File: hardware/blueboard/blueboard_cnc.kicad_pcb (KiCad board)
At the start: 2 copper layers, 199.4 x 198.9 mm, 105 parts, among them SW1 SW_SPST

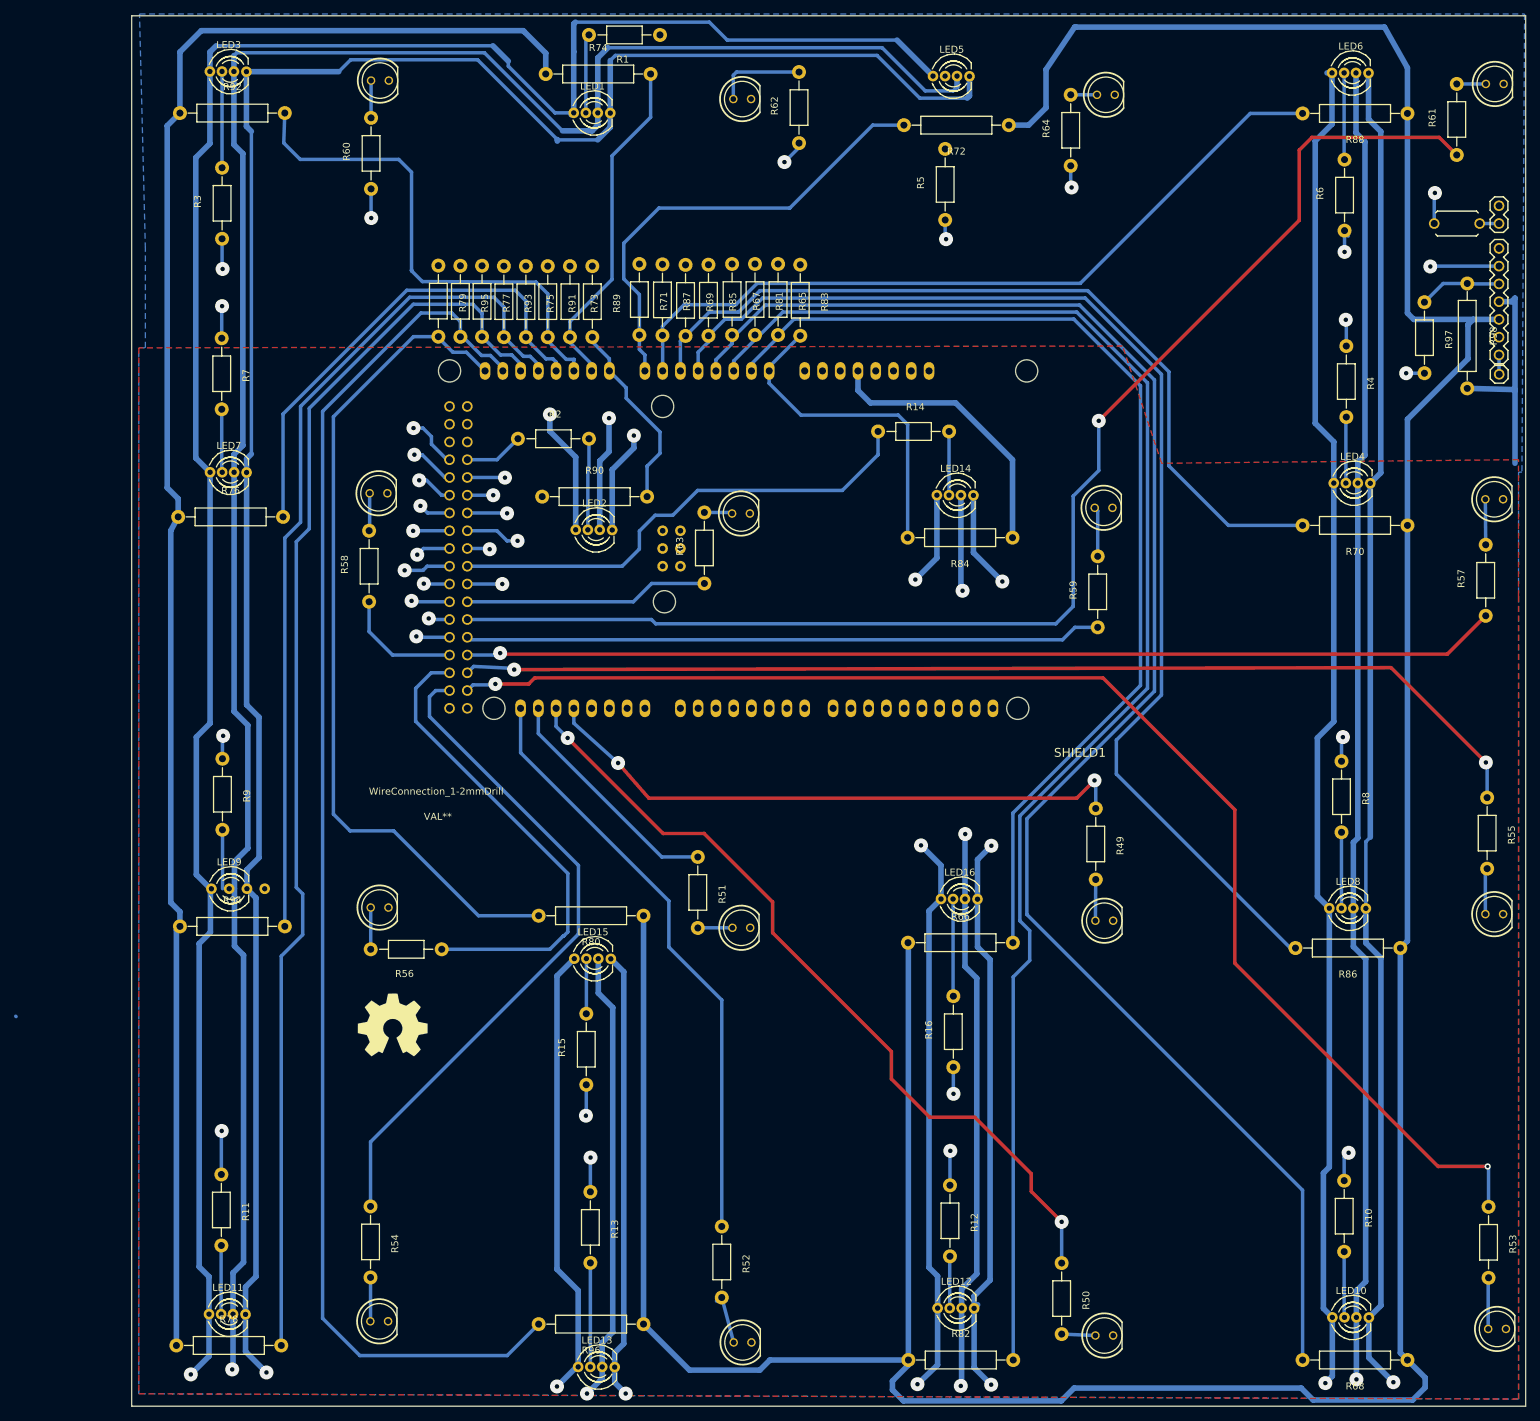
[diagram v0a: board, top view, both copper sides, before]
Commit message: state when board was cncd
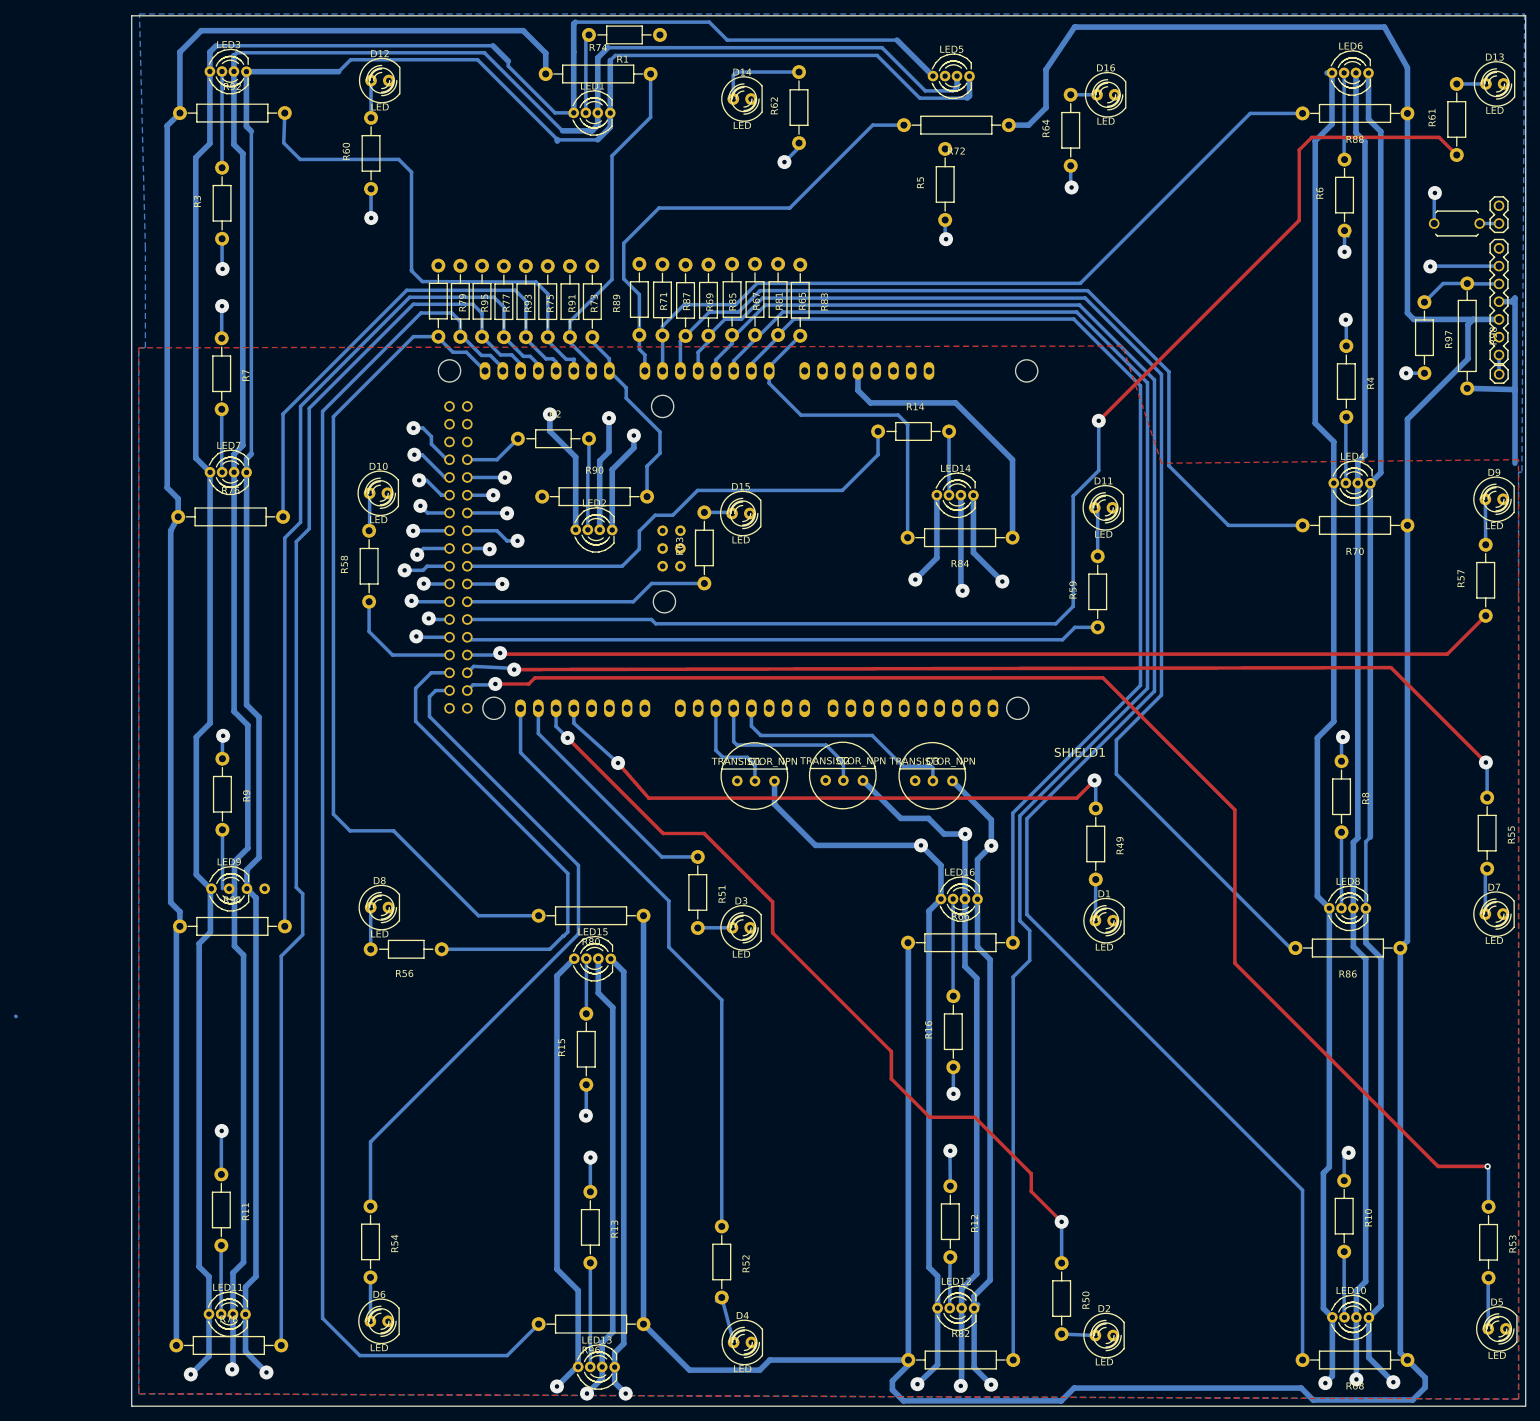
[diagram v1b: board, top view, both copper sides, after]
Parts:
- removed LOGO_OSHW_silkscreen_10mm: val**, Freetronics:LOGO_OSHW_silkscreen_10mm
- removed WireConnection_1-2mmDrill: VAL**, Wire_Connections_Bridges:WireConnection_1-2mmDrill
- added Q1: TRANSISTOR_NPN, finn_kicad:EBC-transistor-NPN, F.Cu at (186.7, 22.1)
- added Q2: TRANSISTOR_NPN, finn_kicad:EBC-transistor-NPN, F.Cu at (199.3, 22.0)
- added Q3: TRANSISTOR_NPN, finn_kicad:EBC-transistor-NPN, F.Cu at (212.1, 22.1)
- D1, D10, D11, D12, D13, D14, D15, D16, D2, D3, D4, D5, D6, D7, D8, D9: footprint Freetronics:LED-5MM -> LEDs:LED-5MM
- R1, R10, R11, R12, R13, R14, R15, R16, R2, R3, R4, R5, R6, R7, R8, R9: value 470 -> 220
- moved R12 0.14 mm to (214.6, 87.9)
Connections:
- R1 pad 2: Net-(LED1-PadA) -> Net-(LED16-PadA)
- R10 pad 2: Net-(LED10-PadA) -> Net-(LED9-PadA)
- R11 pad 2: Net-(LED11-PadA) -> Net-(LED10-PadA)
- R12 pad 2: Net-(LED12-PadA) -> Net-(LED11-PadA)
- R13 pad 1: Net-(R13-Pad1) -> Net-(LED15-PadA)
- R13 pad 2: Net-(LED13-PadA) -> Net-(R13-Pad2)
- R14 pad 1: Net-(R14-Pad1) -> Net-(LED14-PadA)
- R14 pad 2: Net-(LED14-PadA) -> Net-(R14-Pad2)
- R15 pad 1: Net-(R15-Pad1) -> Net-(LED13-PadA)
- R15 pad 2: Net-(LED15-PadA) -> Net-(R15-Pad2)
- R16 pad 1: Net-(R16-Pad1) -> Net-(LED12-PadA)
- R16 pad 2: Net-(LED16-PadA) -> Net-(R16-Pad2)
- R2 pad 2: Net-(LED2-PadA) -> Net-(LED1-PadA)
- R3 pad 2: Net-(LED3-PadA) -> Net-(LED2-PadA)
- R4 pad 2: Net-(LED4-PadA) -> Net-(LED3-PadA)
- R49 pad 2: Net-(D1-PadA) -> Net-(D1-Pad1)
- R5 pad 2: Net-(LED5-PadA) -> Net-(LED4-PadA)
- R50 pad 2: Net-(D2-PadA) -> Net-(D2-Pad1)
- R51 pad 2: Net-(D3-PadA) -> Net-(D3-Pad1)
- R52 pad 2: Net-(D4-PadA) -> Net-(D4-Pad1)
- R53 pad 2: Net-(D5-PadA) -> Net-(D5-Pad1)
- R54 pad 2: Net-(D6-PadA) -> Net-(D6-Pad1)
- R55 pad 2: Net-(D7-PadA) -> Net-(D7-Pad1)
- R56 pad 2: Net-(D8-PadA) -> Net-(D8-Pad1)
- R57 pad 2: Net-(D9-PadA) -> Net-(D9-Pad1)
- R58 pad 2: Net-(D10-PadA) -> Net-(D10-Pad1)
- R59 pad 2: Net-(D11-PadA) -> Net-(D11-Pad1)
- R6 pad 2: Net-(LED6-PadA) -> Net-(LED5-PadA)
- R60 pad 2: Net-(D12-PadA) -> Net-(D12-Pad1)
- R61 pad 2: Net-(D13-PadA) -> Net-(D13-Pad1)
- R62 pad 2: Net-(D14-PadA) -> Net-(D14-Pad1)
- R63 pad 2: Net-(D15-PadA) -> Net-(D15-Pad1)
- R64 pad 2: Net-(D16-PadA) -> Net-(D16-Pad1)
- R7 pad 2: Net-(LED7-PadA) -> Net-(LED6-PadA)
- R8 pad 2: Net-(LED8-PadA) -> Net-(LED7-PadA)
- R9 pad 2: Net-(LED9-PadA) -> Net-(LED8-PadA)
- SHIELD1 pad 34: Net-(R16-Pad1) -> Net-(R13-Pad2)
- SHIELD1 pad 35: Net-(R15-Pad1) -> Net-(R14-Pad2)
- SHIELD1 pad 36: Net-(R14-Pad1) -> Net-(R15-Pad2)
- SHIELD1 pad 37: Net-(R13-Pad1) -> Net-(R16-Pad2)
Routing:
- net Net-(LED9-PadA): track 8.43 -> 92.4 mm
- net B: track 682.3 -> 608.0 mm
- net Net-(R14-Pad1): track 70.2 -> 0.00 mm
- net Net-(LED14-PadA): track 9.12 -> 57.1 mm
- net Net-(Q3-PadB): track 0.00 -> 32.9 mm
- net Net-(R15-Pad2): track 0.00 -> 30.0 mm
- net R: track 689.6 -> 716.4 mm
- net Net-(Q2-PadB): track 0.00 -> 24.3 mm
- net G: track 679.8 -> 700.4 mm
- net Net-(Q1-PadB): track 0.00 -> 14.8 mm
- net Net-(D14-PadA): track 13.2 -> 0.00 mm
- net Net-(D14-Pad1): track 0.00 -> 13.2 mm
- net Net-(R13-Pad1): track 11.6 -> 0.00 mm, vias 2 -> 0
- net Net-(LED10-PadA): track 9.41 -> 0.23 mm
- net Net-(R16-Pad1): track 8.99 -> 0.00 mm, vias 2 -> 0
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
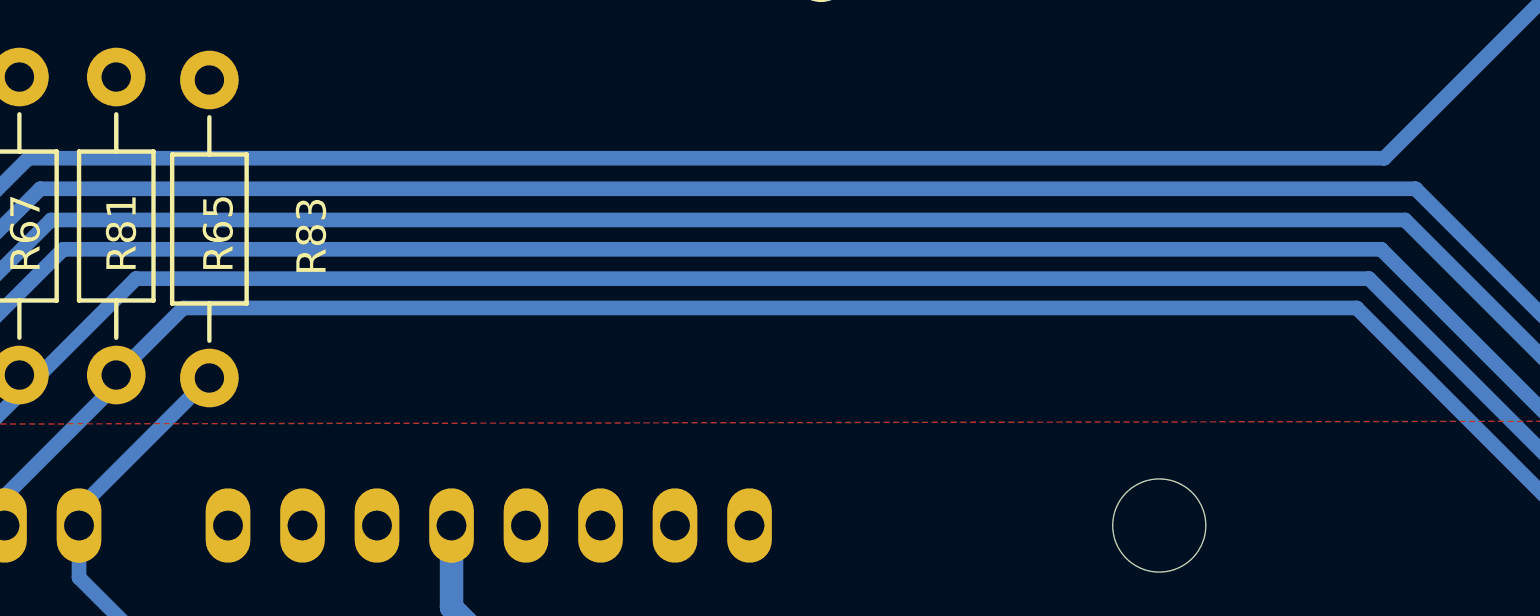
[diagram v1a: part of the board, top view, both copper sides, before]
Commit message: prior to starting over on cnc board
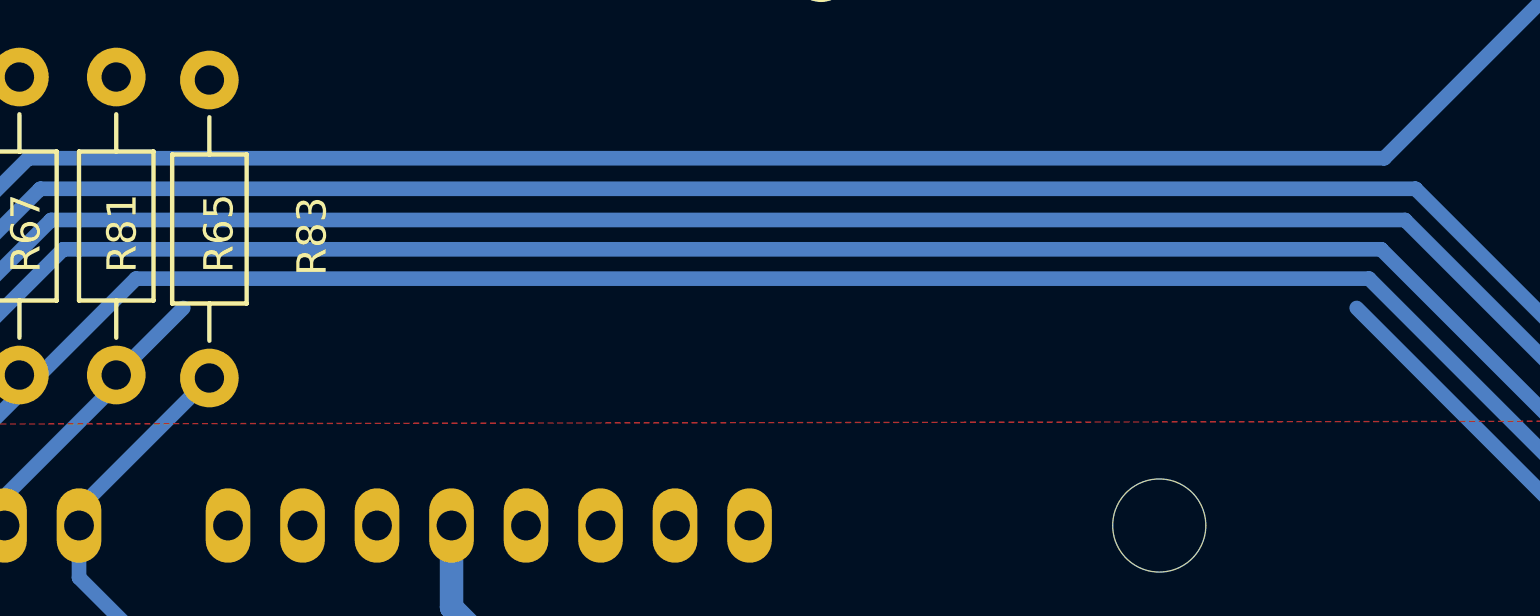
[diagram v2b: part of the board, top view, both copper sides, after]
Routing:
- net B: track 608.0 -> 686.9 mm
- net Net-(LED9-PadA): track 92.4 -> 21.4 mm
- net Net-(LED14-PadA): track 57.1 -> 12.4 mm
- net Net-(R15-Pad2): track 30.0 -> 74.7 mm
- net Net-(R65-Pad2): track 151.3 -> 111.3 mm
- net G: track 700.4 -> 692.6 mm
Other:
- net class Default: clearance 0.5 -> 1.2; trace_width 0.5 -> 1
- net class Power: clearance 0.5 -> 1.2; trace_width 0.8 -> 1
- net class RGB: clearance 0.5 -> 1.2; trace_width 0.8 -> 1
- rule trace_clearance: 0.5 -> 1.2
